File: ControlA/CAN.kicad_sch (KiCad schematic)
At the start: 0 parts

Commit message: usb control
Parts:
- added C? (x2): C, symbol Device:C
- added C?: 2u2, symbol Device:C
- added CN?: PH-4A_RHOS, symbol PH-4A:PH-4A_RHOS
- added R? (x3): R, symbol Device:R
- added R?: 10K, symbol Device:R
- added U?: ESDCAN24-2BLY, SOT_24-2BLY_STM, symbol ESDCAN24-2BLY:ESDCAN24-2BLY
- added U?: SN65HVD230D, SN65HVD230D:SOIC127P599X175-8N, symbol SN65HVD230D:SN65HVD230D
- added U?: 744227S, SMD_227S_WRE, symbol 744227S:744227S
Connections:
- new net: CN?.2, U?.1
- new net: CN?.3, U?.2
- new net: R?.1, R?.1
- new net: C?.2, R?.1, R?.2
- new net: C?.2, U?.3 (VCC)
- new net: U?.4, U?.6 (CANL)
- new net: U?.3, U?.7 (CANH)
- new net: R?.2, U?.8 (RS)
- new net: R?.2, U?.1
- new net: R?.2, U?.2
- new net +3V3: C?.1
- new net +5V: CN?.4
- new net CAN_RX: U?.4 (R)
- new net CAN_TX: U?.1 (D)
- new net GND: C?.1, C?.2, CN?.1, R?.1, U?.2 (GND), U?.3
- no-connect marks 0 -> 1
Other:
- note added: "BYPASS PLACE AS CLOSE AS POSSIBLE TO THE IC"
- note added: "CAN"
- note added: "CAN_H AND CAN_L TO BE ROUTED AS DIFFERENTIAL PAIR"
- note added: "MODE SELECTION RESISTOR SLEW RATE OF-15 V/µS MORE INFO ON DATASHEET"

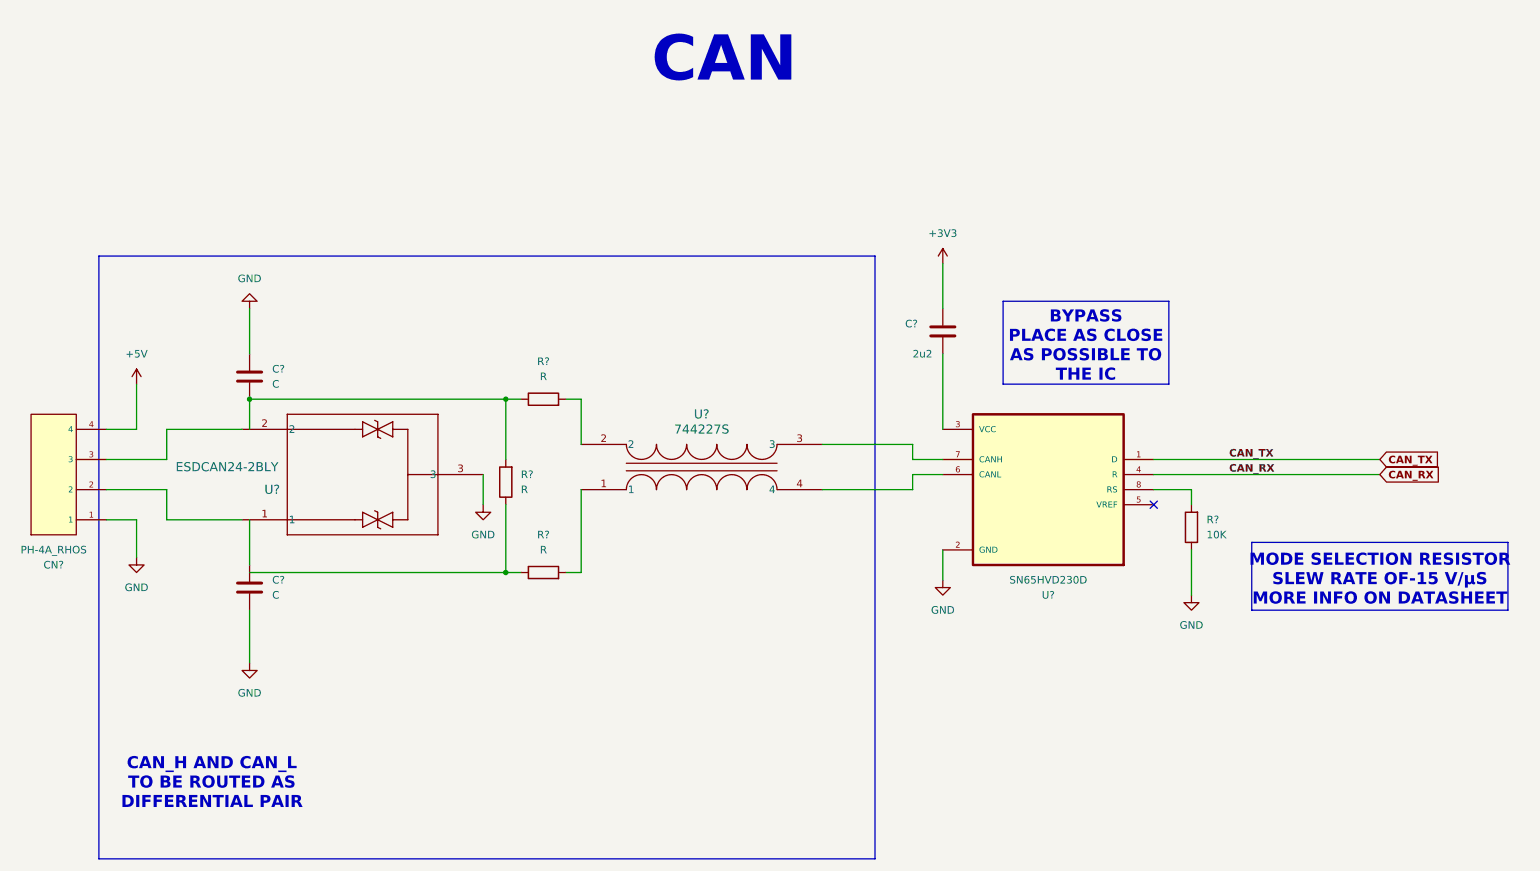
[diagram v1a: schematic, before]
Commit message: final shema symbole
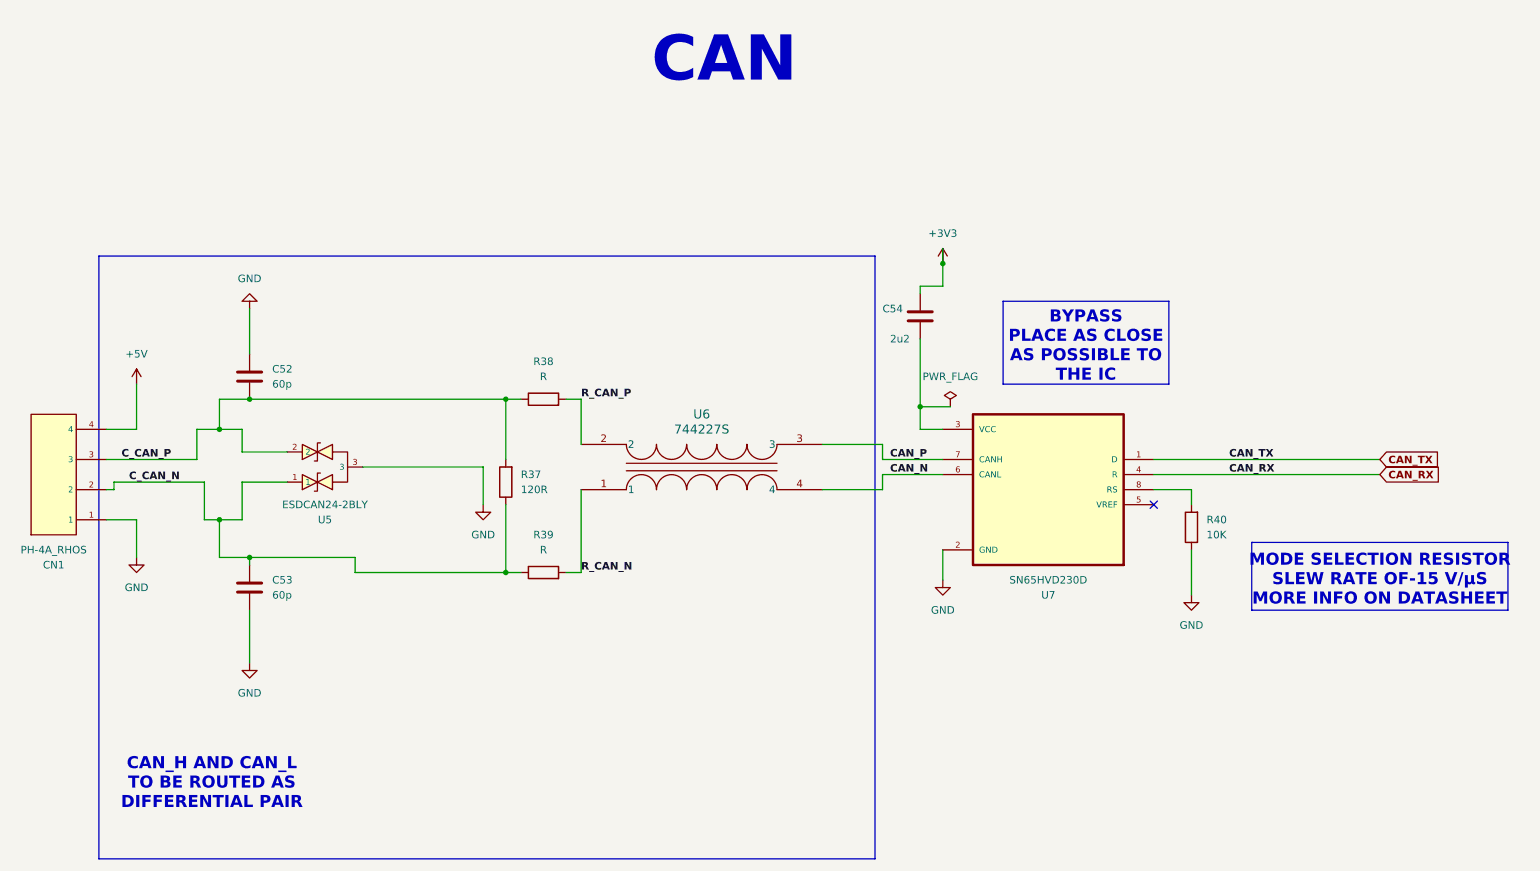
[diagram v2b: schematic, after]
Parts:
- removed U?: ESDCAN24-2BLY, SOT_24-2BLY_STM, symbol ESDCAN24-2BLY:ESDCAN24-2BLY
- added U5: ESDCAN24-2BLY, footprint:SOT-23-3_L3.0-W1.7-P0.95-LS2.9-BR, symbol ESDCAN24-2BLY:ESDCAN24-2BLY
- C52, C53: renamed from C?; value C -> 60p; footprint (none) -> Capacitor_SMD:C_0805_2012Metric
- C54: renamed from C?; footprint (none) -> Capacitor_SMD:C_0805_2012Metric
- CN1: renamed from CN?; footprint (none) -> footprint:CONN-TH_PH-4A
- R37: renamed from R?; value R -> 120R; footprint (none) -> Resistor_SMD:R_0805_2012Metric
- R38, R39, R40: renamed from R?; footprint (none) -> Resistor_SMD:R_0805_2012Metric
- U6: renamed from U?; footprint SMD_227S_WRE -> footprint:SMD_227S_WRE-M
- U7: renamed from U?; footprint SN65HVD230D:SOIC127P599X175-8N -> footprint:SOIC127P599X175-8N
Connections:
- net GND: now also U5.3
- net C_CAN_N: now reaches C53.1
- net C_CAN_N: now also CN1.2, R37.1, R39.1, U5.1
- net C_CAN_P: now reaches CN1.3
- net C_CAN_P: now also C52.2, R37.2, R38.1, U5.2
- net CAN_N: now reaches U6.4, U7.6 (CANL)
- net CAN_P: now reaches U6.3, U7.7 (CANH)
- net R_CAN_N: now reaches R39.2, U6.1
- net R_CAN_P: now reaches R38.2, U6.2
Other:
- moved on the sheet: C54

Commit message: CHANGE V11
change v1
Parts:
- C52, C53, C54: footprint Capacitor_SMD:C_0805_2012Metric -> Capacitor_SMD:C_0603_1608Metric
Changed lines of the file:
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@@
 			)
 		)
-		(property "Footprint" "Capacitor_SMD:C_0805_2012Metric"
+		(property "Footprint" "Capacitor_SMD:C_0603_1608Metric"
 			(at 54.3052 120.65 0)
 			(effects
@@
 			)
 		)
-		(property "Footprint" "Capacitor_SMD:C_0805_2012Metric"
+		(property "Footprint" "Capacitor_SMD:C_0603_1608Metric"
 			(at 167.3352 74.93 0)
 			(effects
@@
 			)
 		)
-		(property "Footprint" "Capacitor_SMD:C_0805_2012Metric"
+		(property "Footprint" "Capacitor_SMD:C_0603_1608Metric"
 			(at 54.3052 85.09 0)
 			(effects
